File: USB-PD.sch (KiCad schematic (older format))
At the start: 54 parts, among them IC3 TPS7A0518PDBVT, J1 1053131102, J11 E8124-015-01, Q10 Si7223DN, Q11 Si7223DN, Q9 SQS401EN-T1_BE3, U12 STUSB4500QTR, U14 LTC4418IUF#PBF

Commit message: All routes connected
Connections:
- net at U14.6 (~VALID1): now also D37.2; no longer D36.2
- net at U14.7 (~VALID2): now also D36.2; no longer D37.2
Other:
- moved on the sheet: D36, D37, R168, R169
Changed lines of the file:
@@
 L sc606-baseboard:KP-1608EC D?
 U 1 1 62106E33
-P 9650 8200
+P 9650 8300
 AR Path="/61D43102/62106E33" Ref="D?"  Part="1"
 AR Path="/61D49FDE/62106E33" Ref="D?"  Part="1"
 AR Path="/623AED4D/62106E33" Ref="D36"  Part="1"
-F 0 "D36" H 9600 7953 60  0000 C CNN
-F 1 "KP-1608EC" H 9600 8059 60  0000 C CNN
-F 2 "sc606-baseboard-footprints:LED_0603" H 9850 8400 60  0001 L CNN
-F 3 "https://www.farnell.com/datasheets/1854072.pdf" H 9850 8500 60  0001 L CNN
-F 4 "KP-1608EC" H 9850 8700 60  0001 L CNN "MPN"
-F 5 "KINGBRIGHT" H 9860 8820 60  0001 L CNN "Manufacturer"
-	1    9650 8200
+F 0 "D36" H 9600 8053 60  0000 C CNN
+F 1 "KP-1608EC" H 9600 8159 60  0000 C CNN
+F 2 "sc606-baseboard-footprints:LED_0603" H 9850 8500 60  0001 L CNN
+F 3 "https://www.farnell.com/datasheets/1854072.pdf" H 9850 8600 60  0001 L CNN
+F 4 "KP-1608EC" H 9850 8800 60  0001 L CNN "MPN"
+F 5 "KINGBRIGHT" H 9860 8920 60  0001 L CNN "Manufacturer"
+	1    9650 8300
 	-1   0    0    1
 $EndComp
@@
 L sc606-baseboard:KP-1608EC D?
 U 1 1 6211676C
-P 10000 8300
+P 10000 8200
 AR Path="/61D43102/6211676C" Ref="D?"  Part="1"
 AR Path="/61D49FDE/6211676C" Ref="D?"  Part="1"
 AR Path="/623AED4D/6211676C" Ref="D37"  Part="1"
-F 0 "D37" H 9950 8053 60  0000 C CNN
-F 1 "KP-1608EC" H 9950 8159 60  0000 C CNN
-F 2 "sc606-baseboard-footprints:LED_0603" H 10200 8500 60  0001 L CNN
-F 3 "https://www.farnell.com/datasheets/1854072.pdf" H 10200 8600 60  0001 L CNN
-F 4 "KP-1608EC" H 10200 8800 60  0001 L CNN "MPN"
-F 5 "KINGBRIGHT" H 10210 8920 60  0001 L CNN "Manufacturer"
-	1    10000 8300
+F 0 "D37" H 9950 7953 60  0000 C CNN
+F 1 "KP-1608EC" H 9950 8059 60  0000 C CNN
+F 2 "sc606-baseboard-footprints:LED_0603" H 10200 8400 60  0001 L CNN
+F 3 "https://www.farnell.com/datasheets/1854072.pdf" H 10200 8500 60  0001 L CNN
+F 4 "KP-1608EC" H 10200 8700 60  0001 L CNN "MPN"
+F 5 "KINGBRIGHT" H 10210 8820 60  0001 L CNN "Manufacturer"
+	1    10000 8200
 	-1   0    0    1
 $EndComp
@@
 L sc606-baseboard:R_270R_0603 R168
 U 1 1 6201E54F
+P 10500 8300
+F 0 "R168" H 10500 8513 60  0000 C CNN
+F 1 "R_270R_0603" H 10500 8150 60  0001 C CNN
+F 2 "sc606-baseboard-footprints:0603-res" H 10700 8500 60  0001 L CNN
+F 3 "https://industrial.panasonic.com/cdbs/www-data/pdf/RDA0000/AOA0000C304.pdf" H 10500 8300 50  0001 C CNN
+F 4 "Panasonic" H 10700 8700 60  0001 L CNN "Manufacturer"
+F 5 "ERJ3EKF2700V" H 10700 8600 60  0001 L CNN "MPN"
+F 6 "270R" H 10500 8415 50  0000 C CNN "Val"
+	1    10500 8300
+	1    0    0    -1
+$EndComp
+$Comp
+L sc606-baseboard:R_270R_0603 R169
+U 1 1 6201EDA2
 P 10500 8200
-F 0 "R168" H 10500 8413 60  0000 C CNN
+F 0 "R169" H 10500 8077 60  0000 C CNN
 F 1 "R_270R_0603" H 10500 8050 60  0001 C CNN
 F 2 "sc606-baseboard-footprints:0603-res" H 10700 8400 60  0001 L CNN
@@
 F 4 "Panasonic" H 10700 8600 60  0001 L CNN "Manufacturer"
 F 5 "ERJ3EKF2700V" H 10700 8500 60  0001 L CNN "MPN"
-F 6 "270R" H 10500 8315 50  0000 C CNN "Val"
+F 6 "270R" H 10500 7979 50  0000 C CNN "Val"
 	1    10500 8200
 	1    0    0    -1
 $EndComp
-$Comp
-L sc606-baseboard:R_270R_0603 R169
-U 1 1 6201EDA2
-P 10500 8300
-F 0 "R169" H 10500 8177 60  0000 C CNN
-F 1 "R_270R_0603" H 10500 8150 60  0001 C CNN
-F 2 "sc606-baseboard-footprints:0603-res" H 10700 8500 60  0001 L CNN
-F 3 "https://industrial.panasonic.com/cdbs/www-data/pdf/RDA0000/AOA0000C304.pdf" H 10500 8300 50  0001 C CNN
-F 4 "Panasonic" H 10700 8700 60  0001 L CNN "Manufacturer"
-F 5 "ERJ3EKF2700V" H 10700 8600 60  0001 L CNN "MPN"
-F 6 "270R" H 10500 8079 50  0000 C CNN "Val"
-	1    10500 8300
-	1    0    0    -1
-$EndComp
-Wire Wire Line
-	10350 8200 9850 8200
-Wire Wire Line
-	10200 8300 10350 8300
-Wire Wire Line
-	9900 8300 9325 8300
-Wire Wire Line
-	9325 8200 9550 8200
+Wire Wire Line
+	10200 8200 10350 8200
 Text GLabel 10725 8200 2    50   Input ~ 0
 5V0_SYS
-Wire Wire Line
-	10650 8200 10650 8300
-Wire Wire Line
-	10725 8200 10650 8200
-Connection ~ 10650 8200
 Wire Wire Line
 	7800 9100 7800 9350
@@
 Text Notes 2350 950  0    50   ~ 0
 9...20 VDC
+Wire Wire Line
+	9550 8300 9325 8300
+Wire Wire Line
+	9850 8300 10350 8300
+Wire Wire Line
+	9325 8200 9900 8200
+Wire Wire Line
+	10650 8300 10675 8300
+Wire Wire Line
+	10675 8300 10675 8200
+Wire Wire Line
+	10650 8200 10675 8200
+Connection ~ 10675 8200
+Wire Wire Line
+	10675 8200 10725 8200
 $EndSCHEMATC

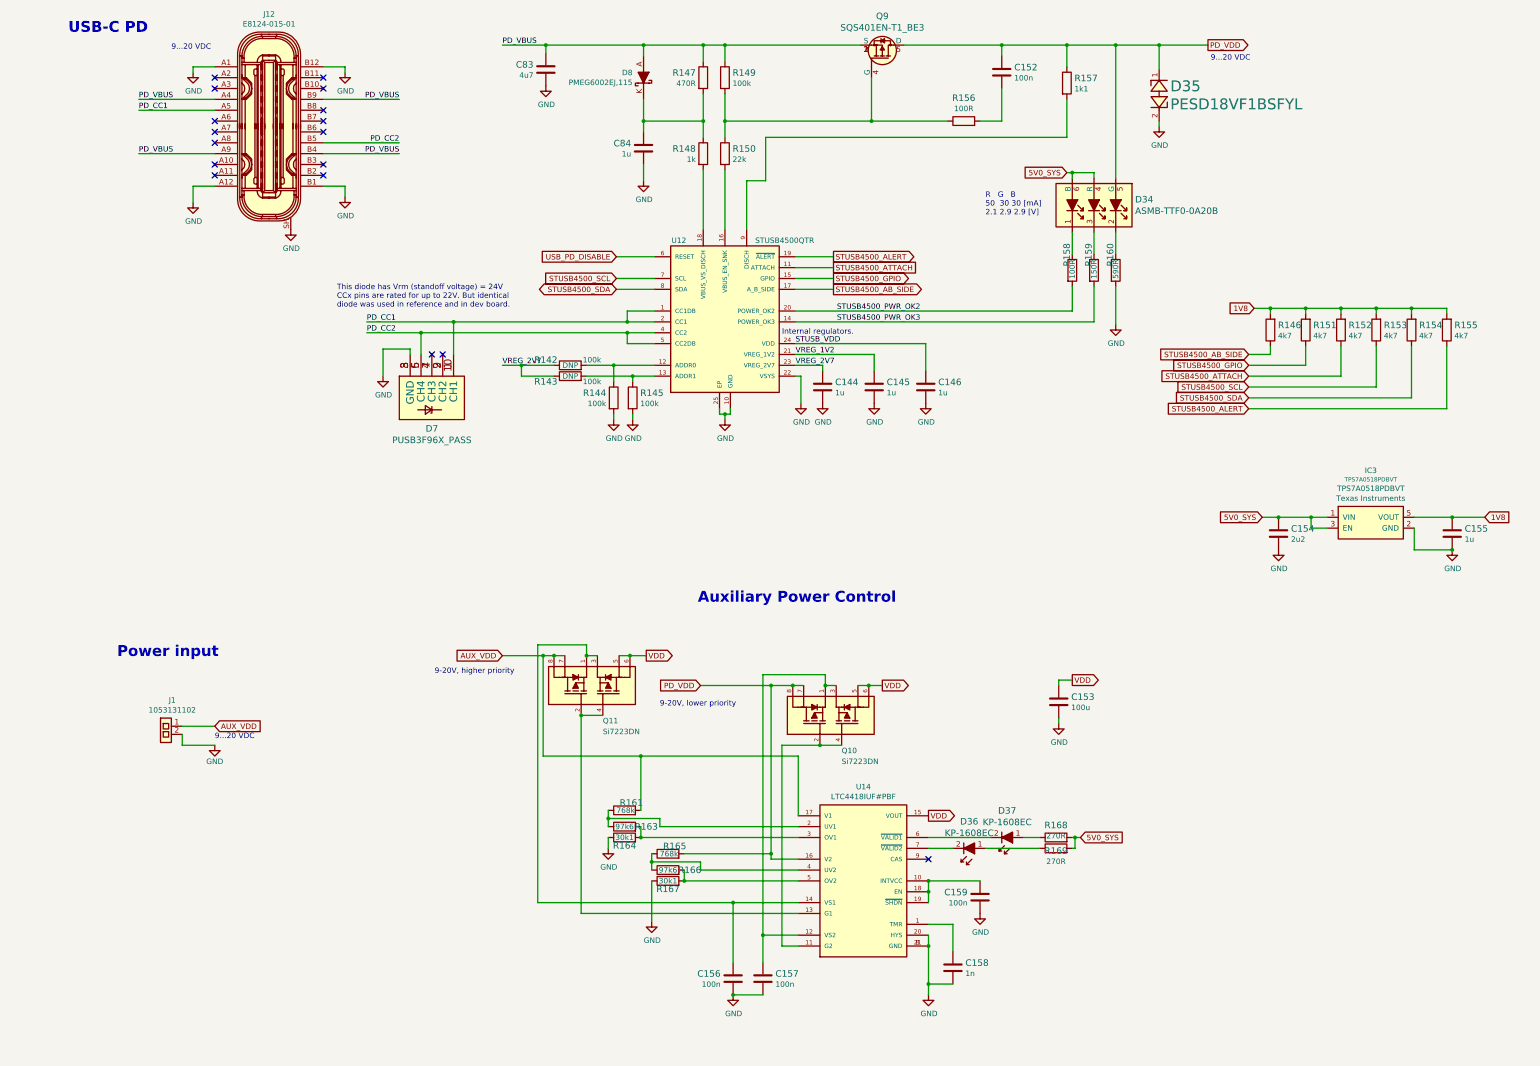
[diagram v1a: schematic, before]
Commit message: Added schema for serial interface connectors
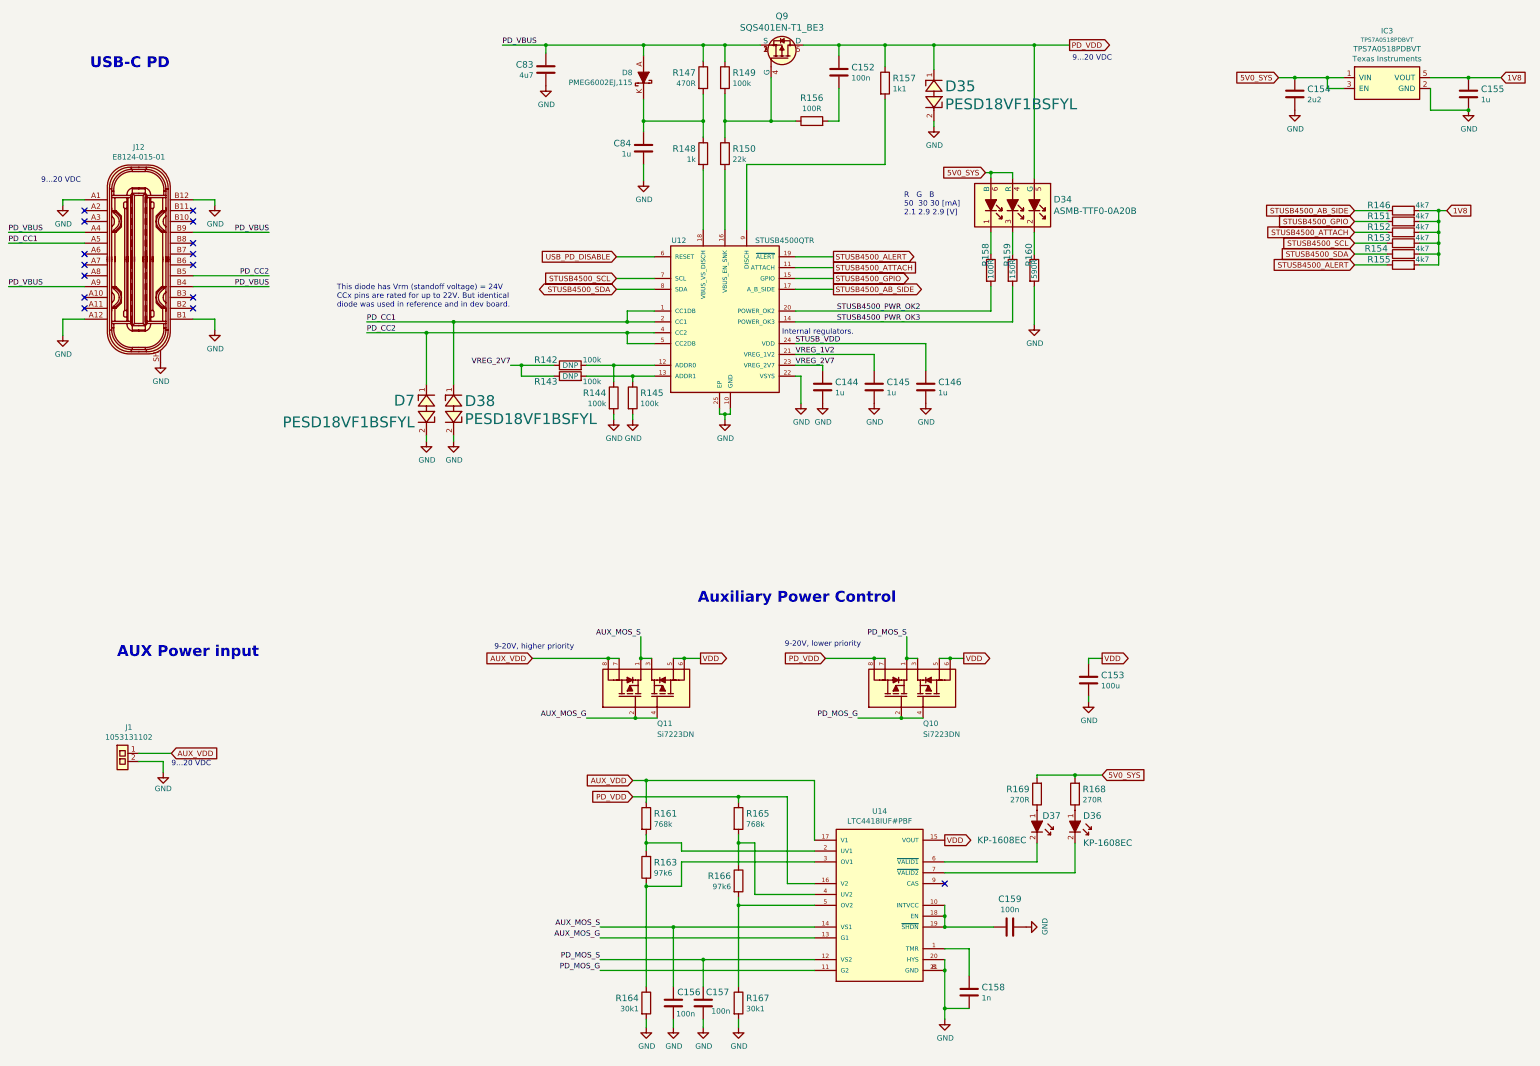
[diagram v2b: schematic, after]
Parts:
- removed D23: PUSB3F96X_PASS, sc606-baseboard-footprints:PUSB3F96X, symbol sc606-baseboard:PUSB3F96X_PASS
- added D38, D7: PESD18VF1BSFYL, sc606-baseboard-footprints:RESC0603X26N, symbol sc606-baseboard:PESD18VF1BSFYL
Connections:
- net AUX_VDD: now also R161.1; no longer R161.2
- net GND: now also R164.2, R167.2, D38.2, D7.2; no longer R164.1, R167.1
- net PD_CC1: now also D38.1
- net PD_CC2: now also D7.1
- net PD_VDD: now also R165.1; no longer R165.2
- net PD_MOS_G: now reaches Q10.2, Q10.4, U14.11 (G2)
- net PD_MOS_S: now reaches C157.2, Q10.1, Q10.3, U14.12 (VS2)
- net AUX_MOS_G: now reaches Q11.2, Q11.4, U14.13 (G1)
- net AUX_MOS_S: now reaches C156.2, Q11.1, Q11.3, U14.14 (VS1)
- net at R166.1, U14.4 (UV2): now also R165.2; no longer R165.1
- net at R166.2, U14.5 (OV2): now also R167.1; no longer R167.2
- new net: R161.2, R163.2, U14.2 (UV1)
- new net: R163.1, R164.1, U14.3 (OV1)
- no-connect marks 17 -> 15
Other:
- note added: "AUX Power input"
- note removed: "Power input"
- moved on the sheet: C152, C153, C154, C155, C156, C157, C158, C159, D34, D35, D36, D37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

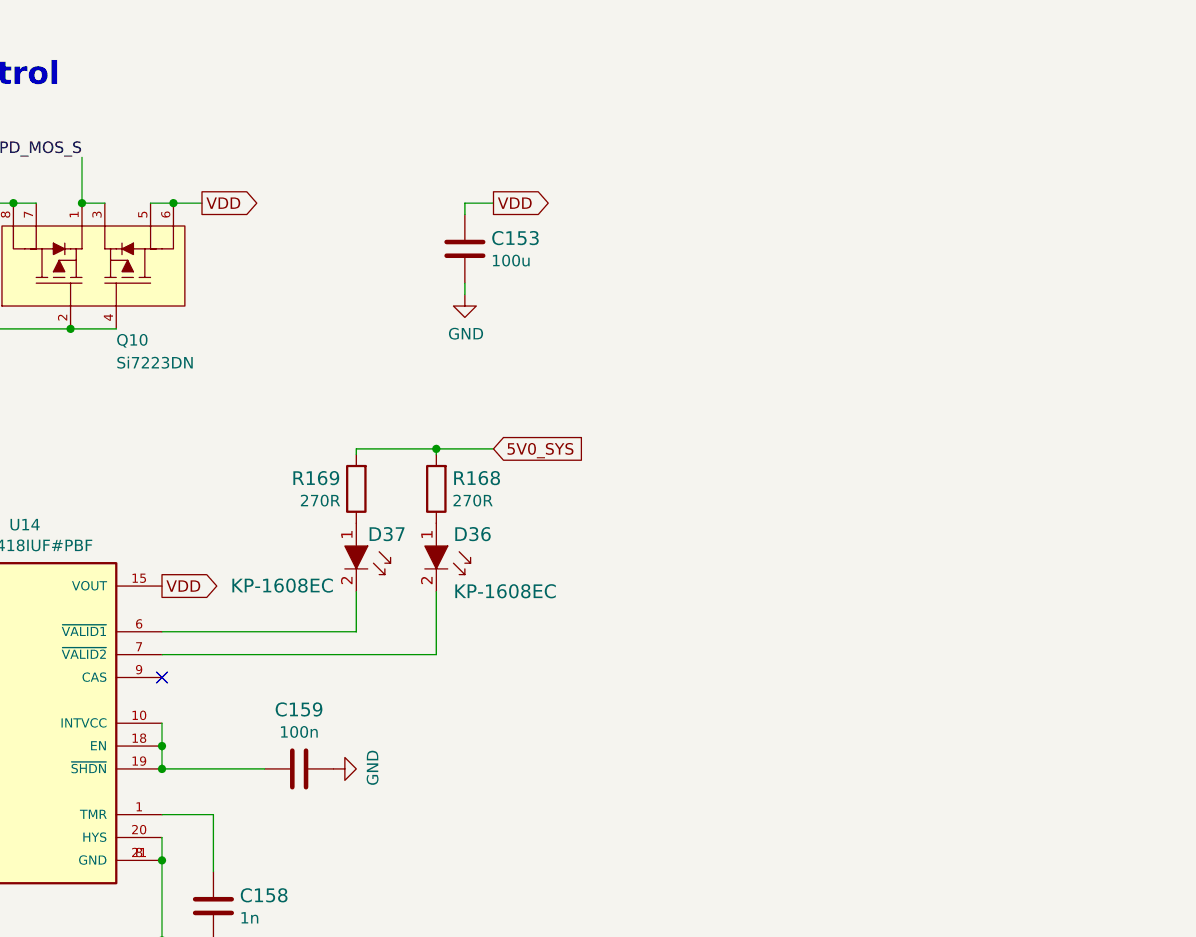
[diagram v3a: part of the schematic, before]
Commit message: Finished board routing
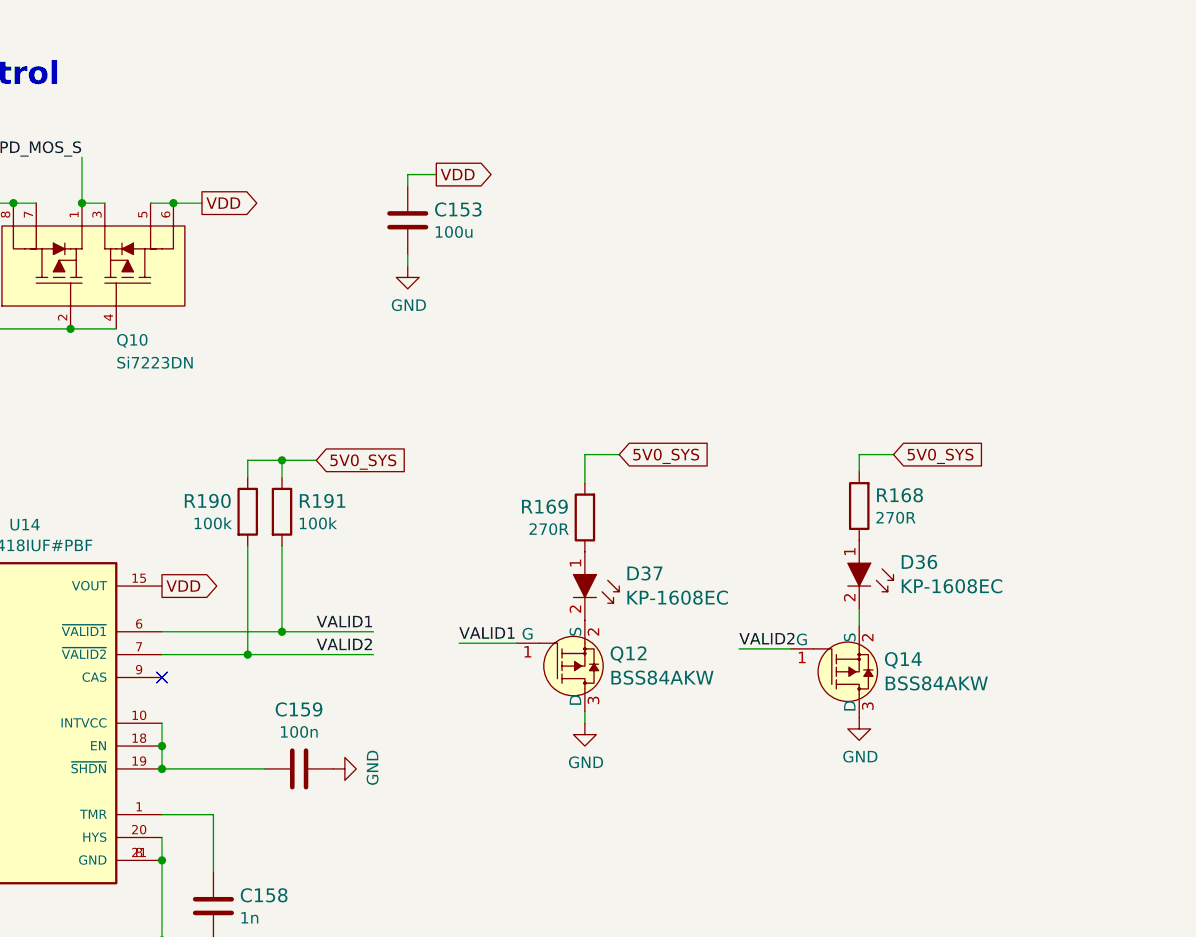
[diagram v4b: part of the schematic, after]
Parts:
- added Q12, Q14: BSS84AKW, antmicro-footprints:SOT-323, symbol antmicroTransistorsFETsMOSFETsSingle:BSS84AKW
- added R190, R191: R_100k_0402, antmicro-footprints:0402-res, symbol antmicroResistors0402:R_100k_0402
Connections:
- net 5V0_SYS: now also R190.1, R191.1
- net GND: now also Q12.3 (D), Q14.3 (D)
- net at D37.2: now also Q12.2 (S); no longer U14.6 (~VALID1)
- net at D36.2: now also Q14.2 (S); no longer U14.7 (~VALID2)
- new net VALID1: Q12.1 (G), R191.2, U14.6 (~VALID1)
- new net VALID2: Q14.1 (G), R190.2, U14.7 (~VALID2)
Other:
- moved on the sheet: C153, D36, D37, R168, R169
